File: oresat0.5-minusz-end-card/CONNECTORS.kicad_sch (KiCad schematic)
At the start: 22 parts, among them J1 J-SAMTEC-TFM-120-01-L-D-RA, J3 Harwin M55-7101242R, J5 Harwin M55-7101242R

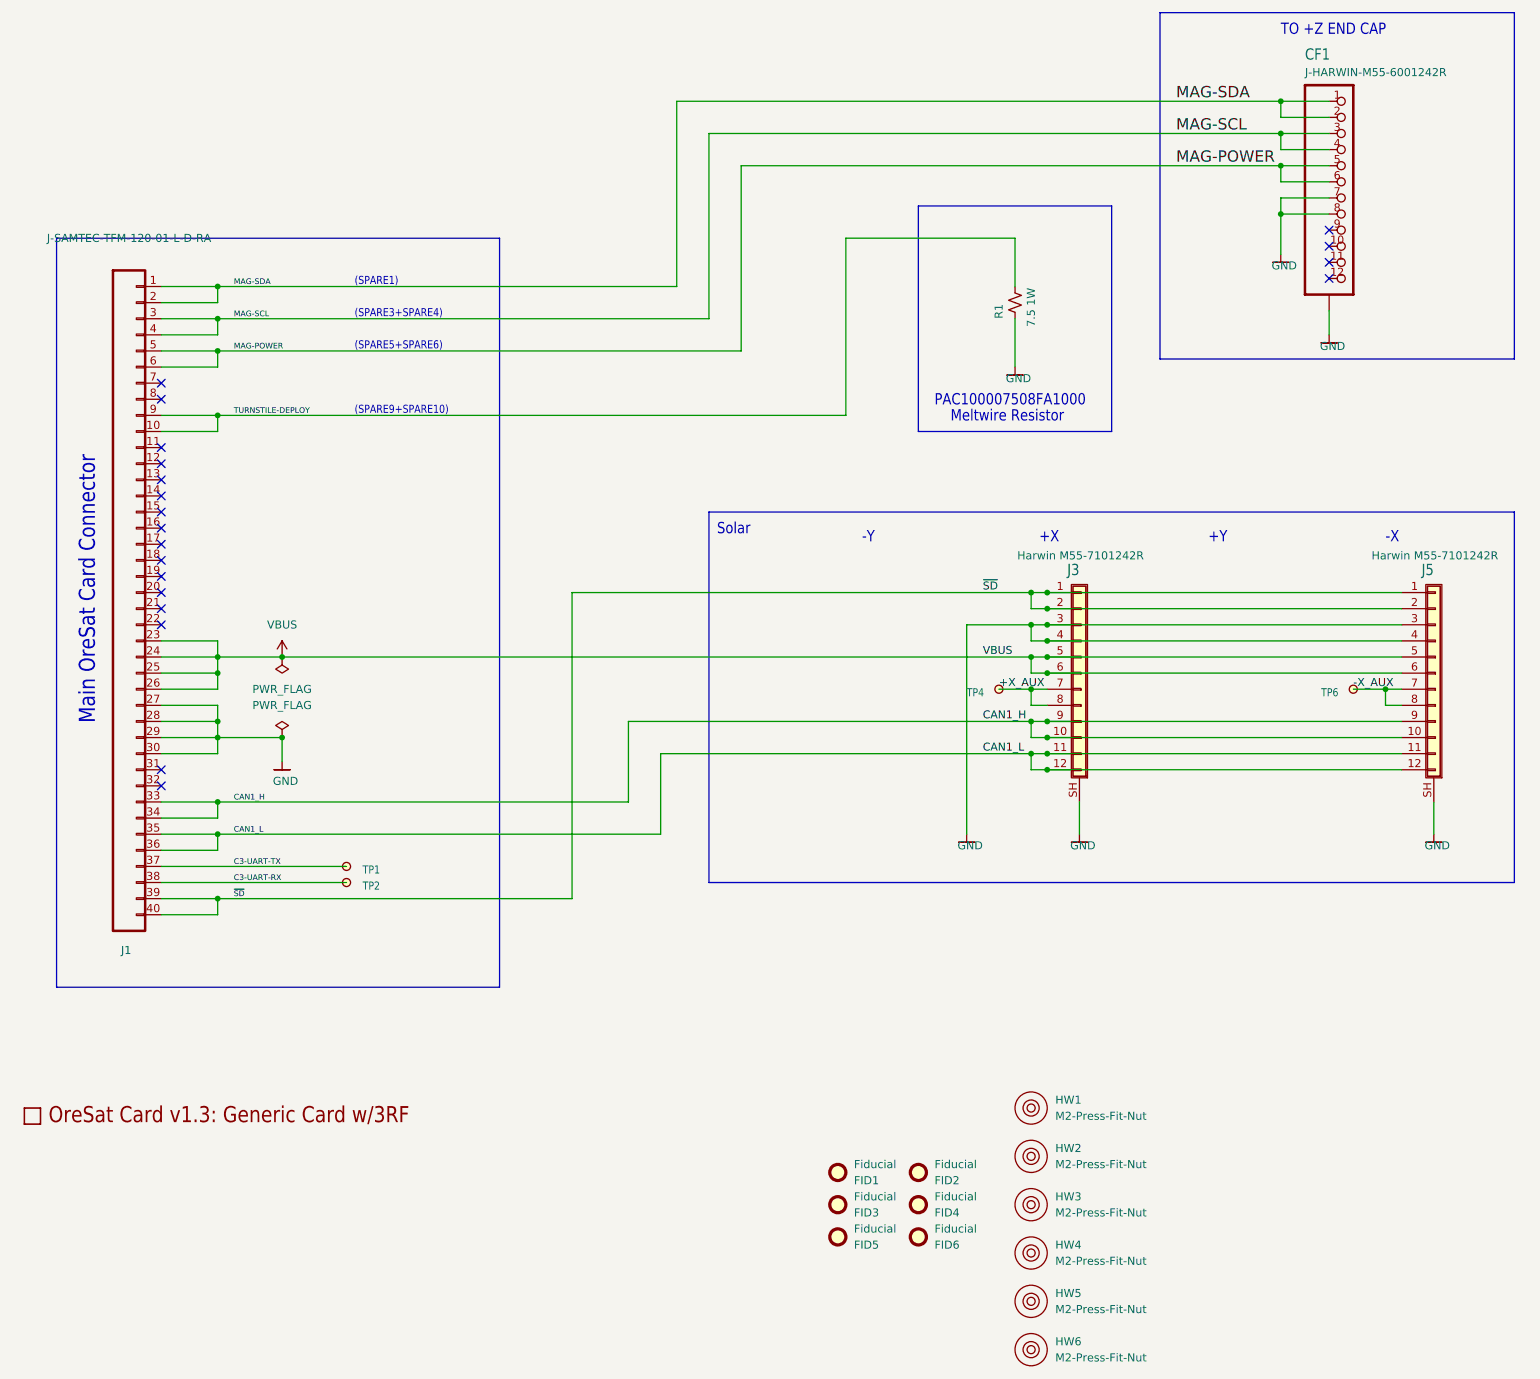
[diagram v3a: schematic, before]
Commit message: Updated OreSat 0.5 end card board outlines and mounting holes, and fixed KiCad library warnings
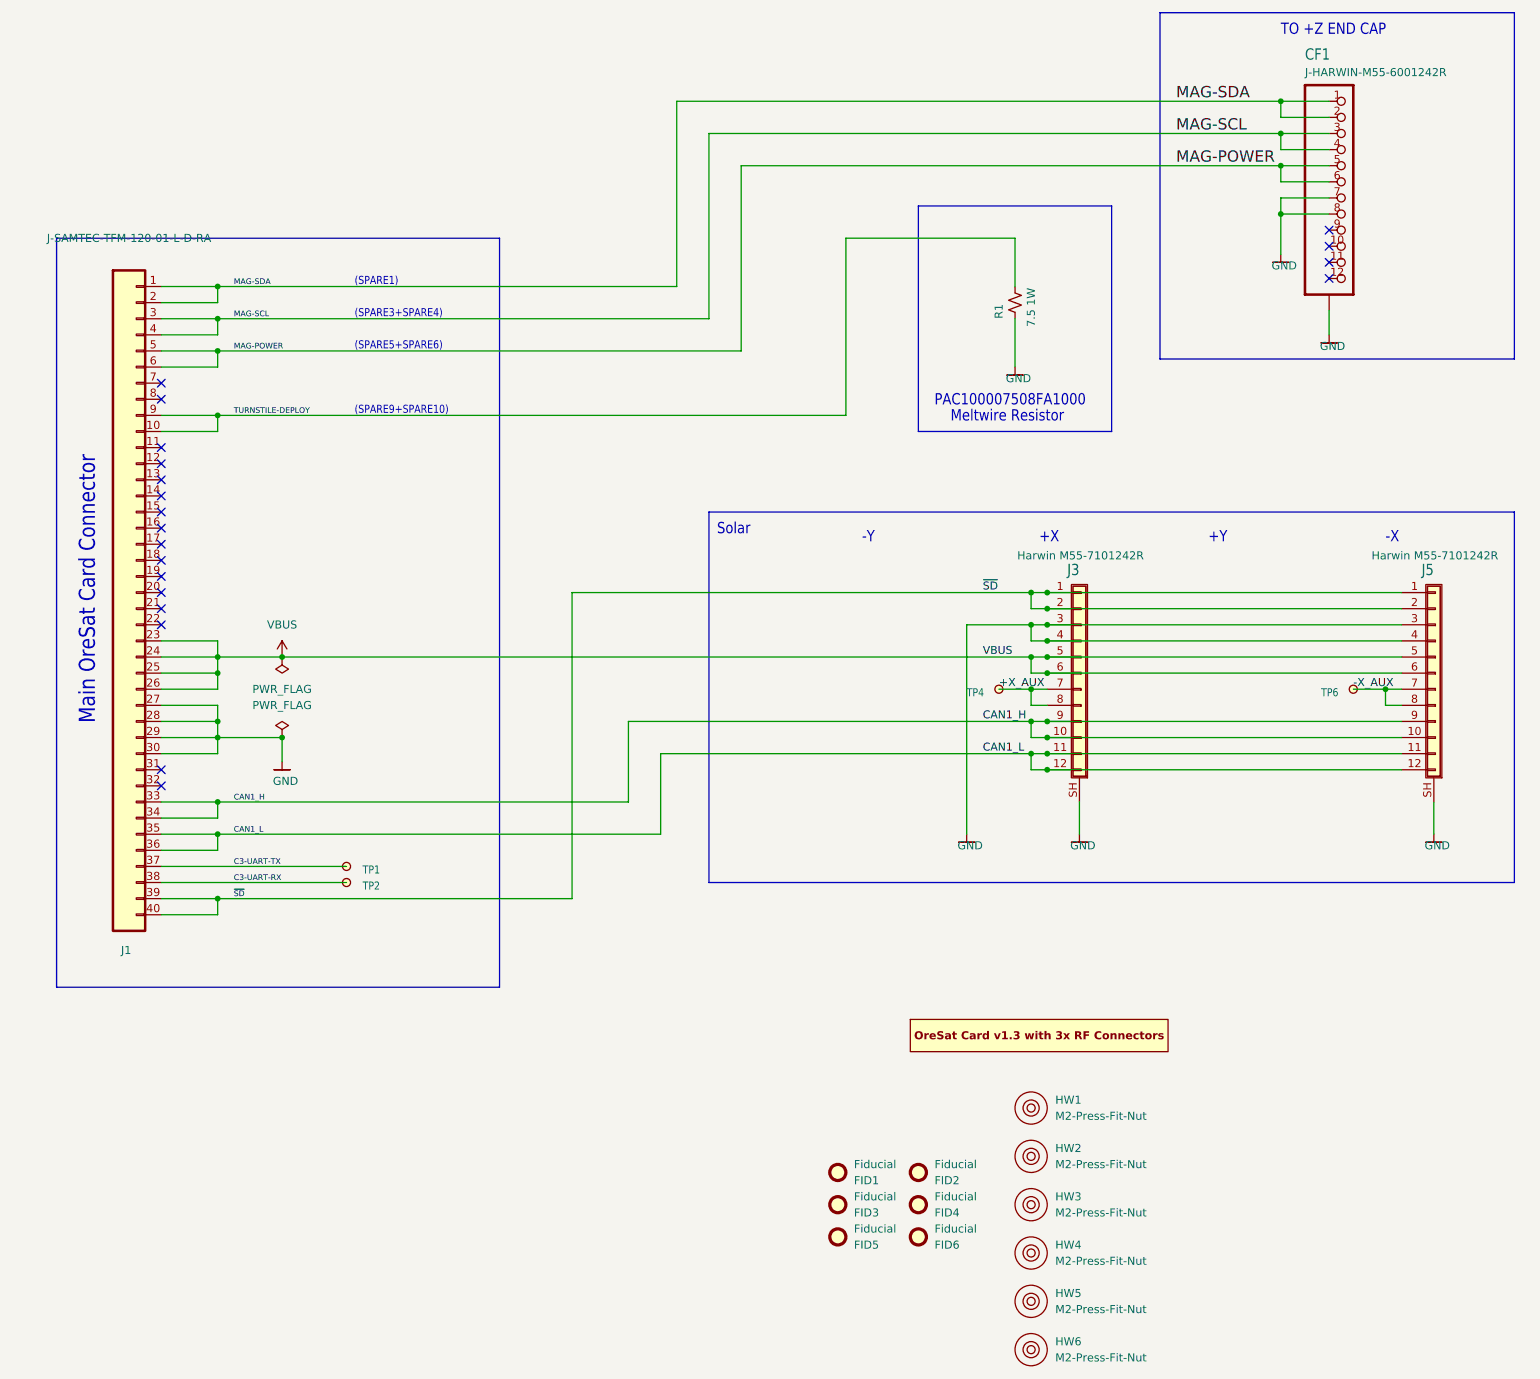
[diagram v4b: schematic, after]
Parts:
- J1: footprint oresat-footprints:J-SAMTEC-TFM-120-X1-XXX-D-RA -> oresat-connectors:J-SAMTEC-TFM-120-X1-XXX-D-RA
- PCB1: footprint plusz-end-card-with-turnstile:ORESAT-CARD-V1.3-GENERIC-3RF -> oresat-pcbs:ORESAT-CARD-V1.3-3RF; symbol plusz-end-card-with-turnstile-eagle-import:ORESAT-CARD-V1.3-GENERIC-3RF -> oresat-pcbs:ORESAT-CARD-V1.3-3RF

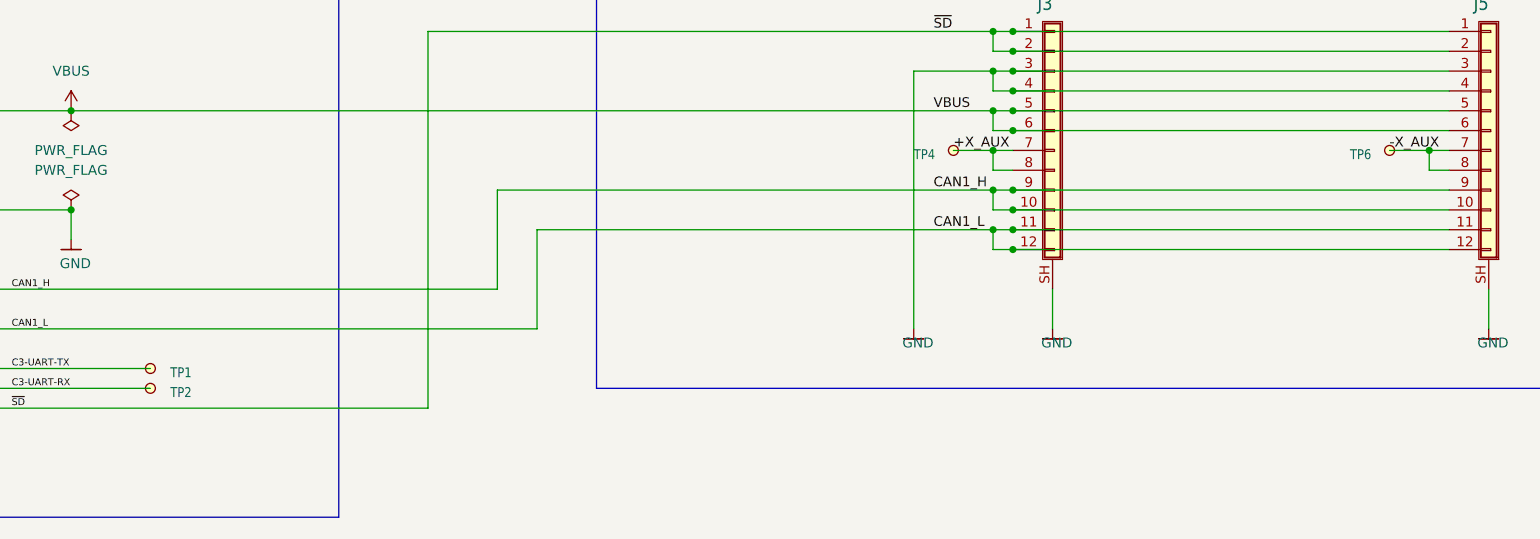
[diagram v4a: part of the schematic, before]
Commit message: Updated -Z end card and DXF
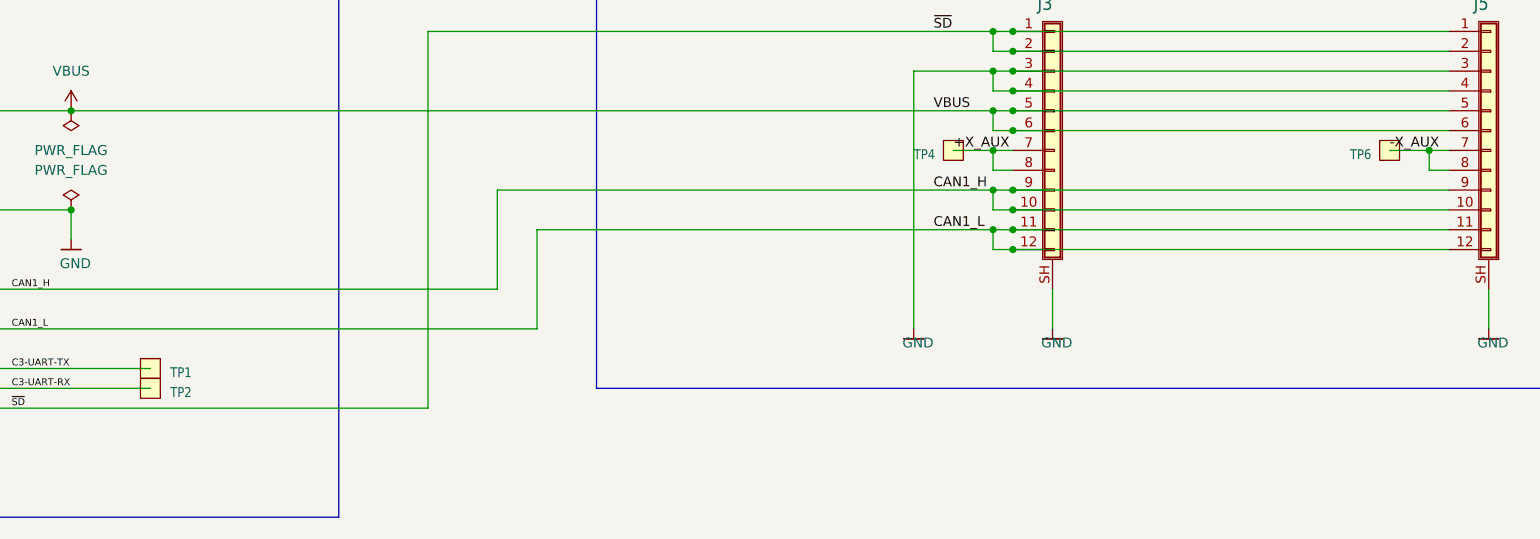
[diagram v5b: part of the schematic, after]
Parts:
- TP1, TP2, TP4, TP6: footprint oresat-misc:TestPoint-MinTH -> oresat-misc:TestPoint-0.75mm-th; symbol oresat-misc:TestPoint-MinTH -> oresat-misc:Test-Point-0.75mm-th
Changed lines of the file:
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@@
     )
   )
-  (symbol (lib_id "oresat-misc:TestPoint-MinTH") (at 185.42 144.78 0) (unit 1)
+  (symbol (lib_id "oresat-misc:Test-Point-0.75mm-th") (at 185.42 144.78 0) (unit 1)
     (in_bom yes) (on_board yes) (dnp no)
     (property "Reference" "TP4" (at 180.34 146.05 0)
@@
       (effects (font (size 1.27 1.27)) hide)
     )
-    (property "Footprint" "oresat-misc:TestPoint-MinTH" (at 185.42 139.7 0)
+    (property "Footprint" "oresat-misc:TestPoint-0.75mm-th" (at 185.42 134.62 0)
       (effects (font (size 1.27 1.27)) hide)
     )
@@
     )
   )
-  (symbol (lib_id "oresat-misc:TestPoint-MinTH") (at 82.55 175.26 0) (unit 1)
+  (symbol (lib_id "oresat-misc:Test-Point-0.75mm-th") (at 82.55 175.26 0) (unit 1)
     (in_bom yes) (on_board yes) (dnp no)
     (property "Reference" "TP2" (at 85.09 176.53 0)
@@
       (effects (font (size 1.27 1.27)) hide)
     )
-    (property "Footprint" "oresat-misc:TestPoint-MinTH" (at 82.55 170.18 0)
+    (property "Footprint" "oresat-misc:TestPoint-0.75mm-th" (at 82.55 165.1 0)
       (effects (font (size 1.27 1.27)) hide)
     )
@@
     )
   )
-  (symbol (lib_id "oresat-misc:TestPoint-MinTH") (at 82.55 172.72 0) (unit 1)
+  (symbol (lib_id "oresat-misc:Test-Point-0.75mm-th") (at 82.55 172.72 0) (unit 1)
     (in_bom yes) (on_board yes) (dnp no)
     (property "Reference" "TP1" (at 85.09 173.99 0)
@@
       (effects (font (size 1.27 1.27)) hide)
     )
-    (property "Footprint" "oresat-misc:TestPoint-MinTH" (at 82.55 167.64 0)
+    (property "Footprint" "oresat-misc:TestPoint-0.75mm-th" (at 82.55 162.56 0)
       (effects (font (size 1.27 1.27)) hide)
     )
@@
     )
   )
-  (symbol (lib_id "oresat-misc:TestPoint-MinTH") (at 241.3 144.78 0) (unit 1)
+  (symbol (lib_id "oresat-misc:Test-Point-0.75mm-th") (at 241.3 144.78 0) (unit 1)
     (in_bom yes) (on_board yes) (dnp no)
     (property "Reference" "TP6" (at 236.22 146.05 0)
@@
       (effects (font (size 1.27 1.27)) hide)
     )
-    (property "Footprint" "oresat-misc:TestPoint-MinTH" (at 241.3 139.7 0)
-      (effects (font (size 1.27 1.27)) hide)
-    )
+    (property "Footprint" "oresat-misc:TestPoint-0.75mm-th" (at 241.3 134.62 0)
+      (effects (font (size 1.27 1.27)) hide)
+    )
